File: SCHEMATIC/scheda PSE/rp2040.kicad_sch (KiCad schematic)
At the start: 26 parts, among them J1 Debug, SW1 RESET_SW, SW2 PROG_SW, U1 RP2040, U2 W25Q16JVUSSQ, U3 AT24C256, Y1 12MHz

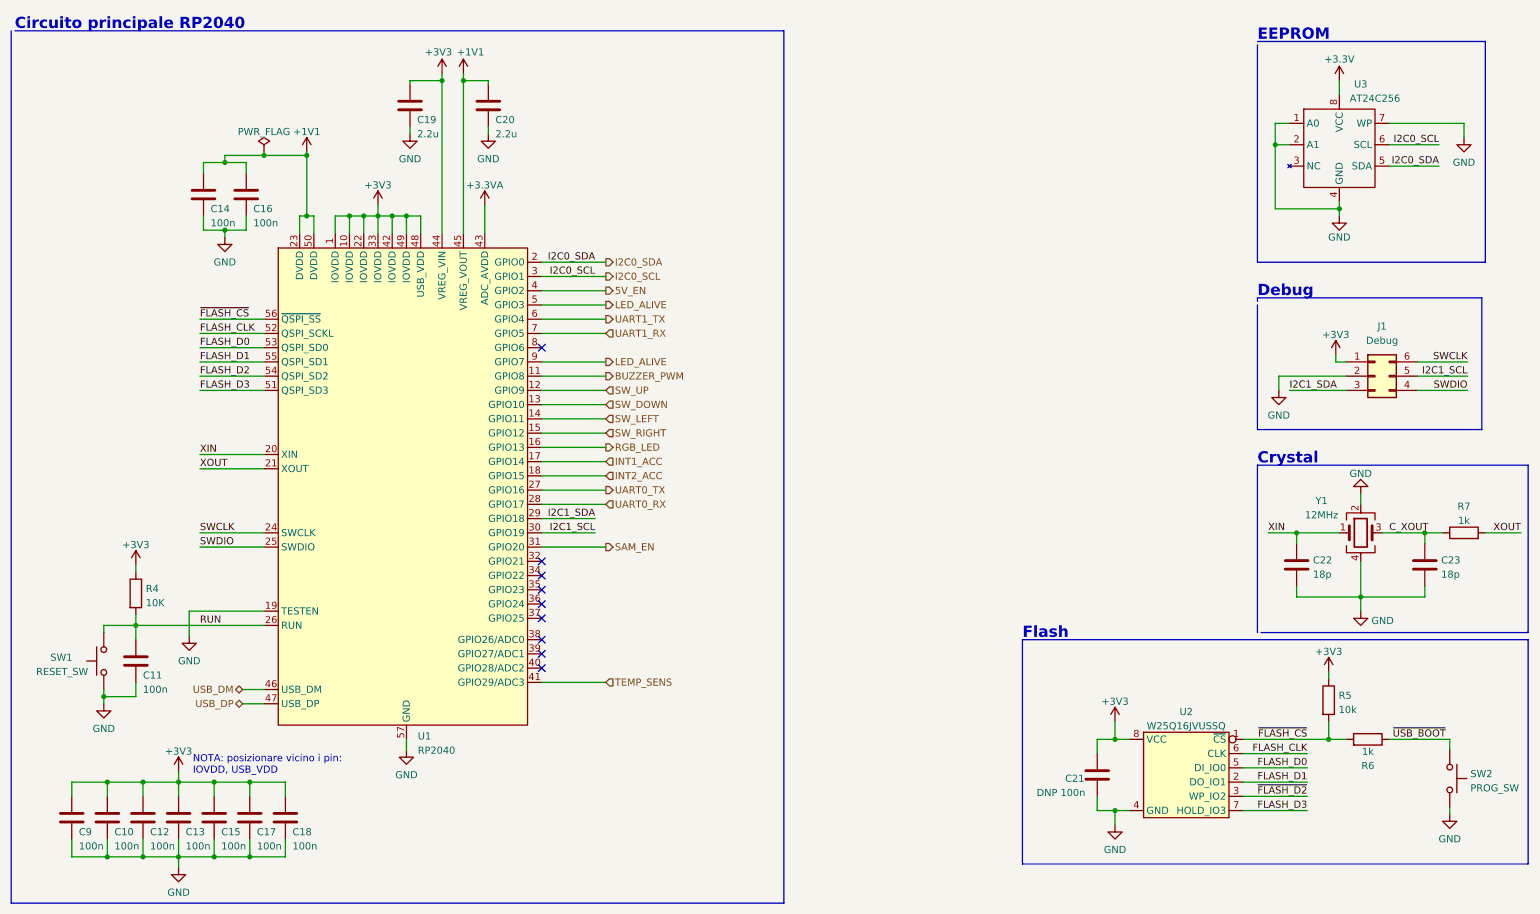
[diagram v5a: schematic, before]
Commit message: iniziato lo broglio. Prima di continuare modificare pin schema
iniziato lo sbroglio della scheda, prima di continuare bisogna sistemare i pin che siano concordi con quelli degli altro (ovvero sistemarli come da tabella su telegram)
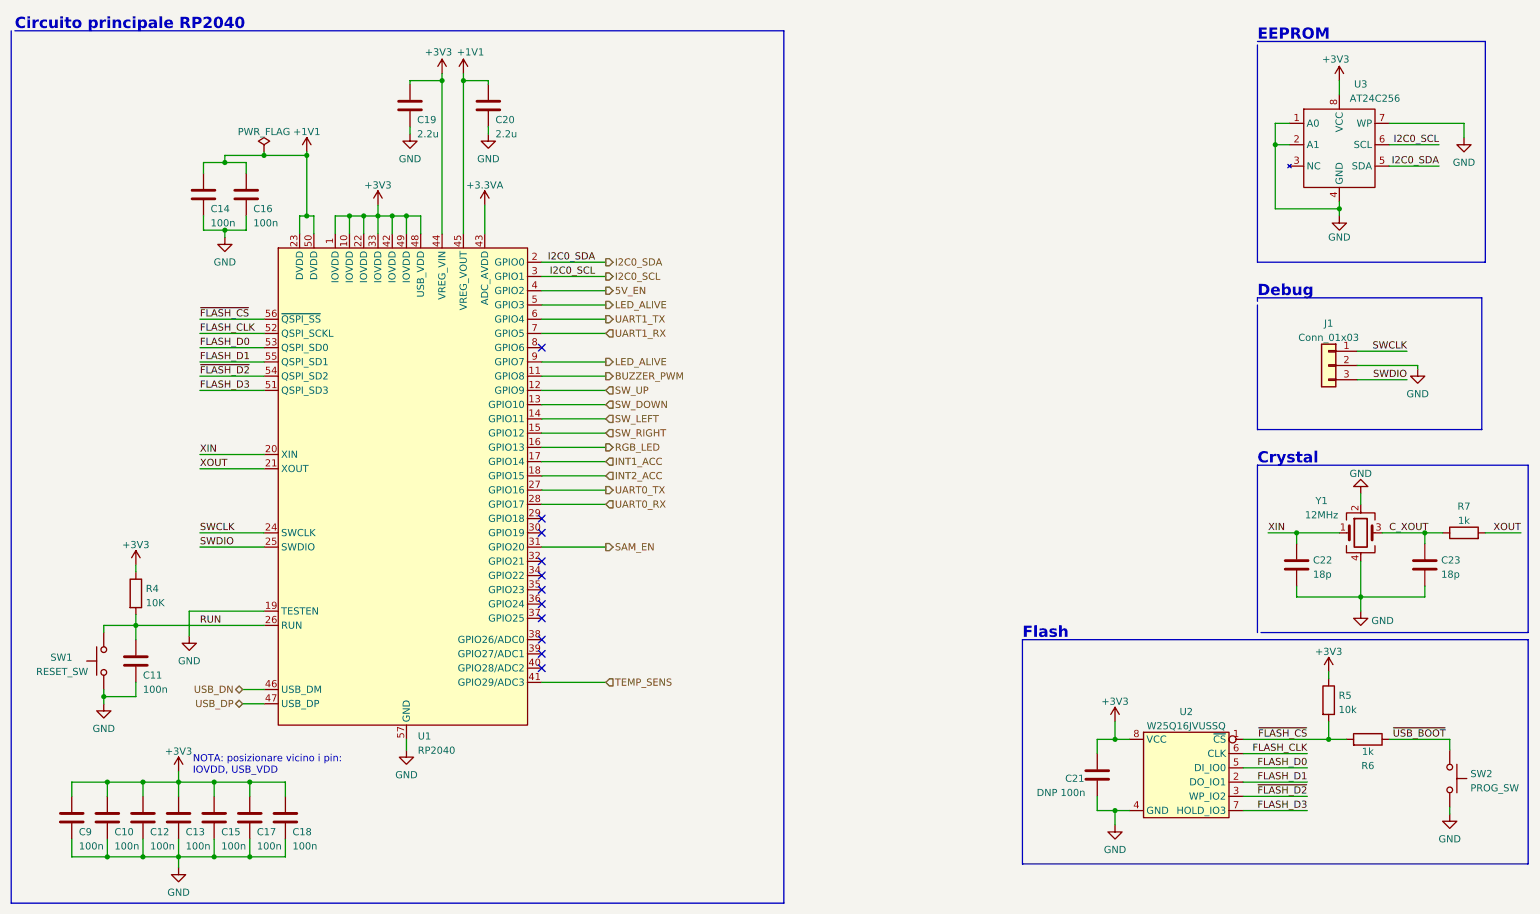
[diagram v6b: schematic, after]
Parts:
- removed J1: Debug, Connector_PinHeader_2.54mm:PinHeader_2x03_P2.54mm_Vertical, symbol Connector_Generic:Conn_02x03_Counter_Clockwise
- added J1: Conn_01x03, Connector_PinHeader_2.54mm:PinHeader_1x03_P2.54mm_Vertical, symbol Connector_Generic:Conn_01x03
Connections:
- net +3.3V is gone; now on net +3V3: U3.8 (VCC)
- net FLASH_D2 is gone; now on net ~{FLASH_D2}: U1.54 (QSPI_SD2)
- net GND: now also J1.2 (Pin_2)
- net SWCLK: now also J1.1 (Pin_1)
- net SWDIO: now also J1.3 (Pin_3)
- net I2C1_SCL: no longer names the net of U1.30 (GPIO19)
- net I2C1_SDA: no longer names the net of U1.29 (GPIO18)
- net USB_DM renamed USB_DN
- no-connect marks 9 -> 11

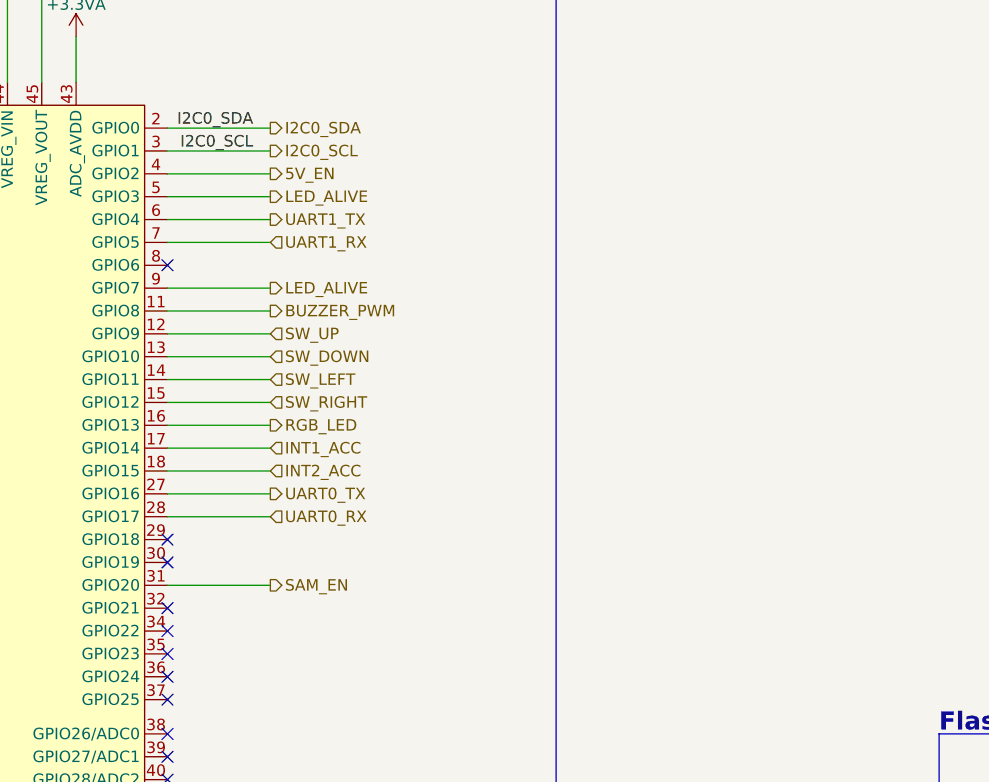
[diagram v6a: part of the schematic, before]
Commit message: modificato pin 2,3,14,15,16,17,18,27,28,29,30,31,32
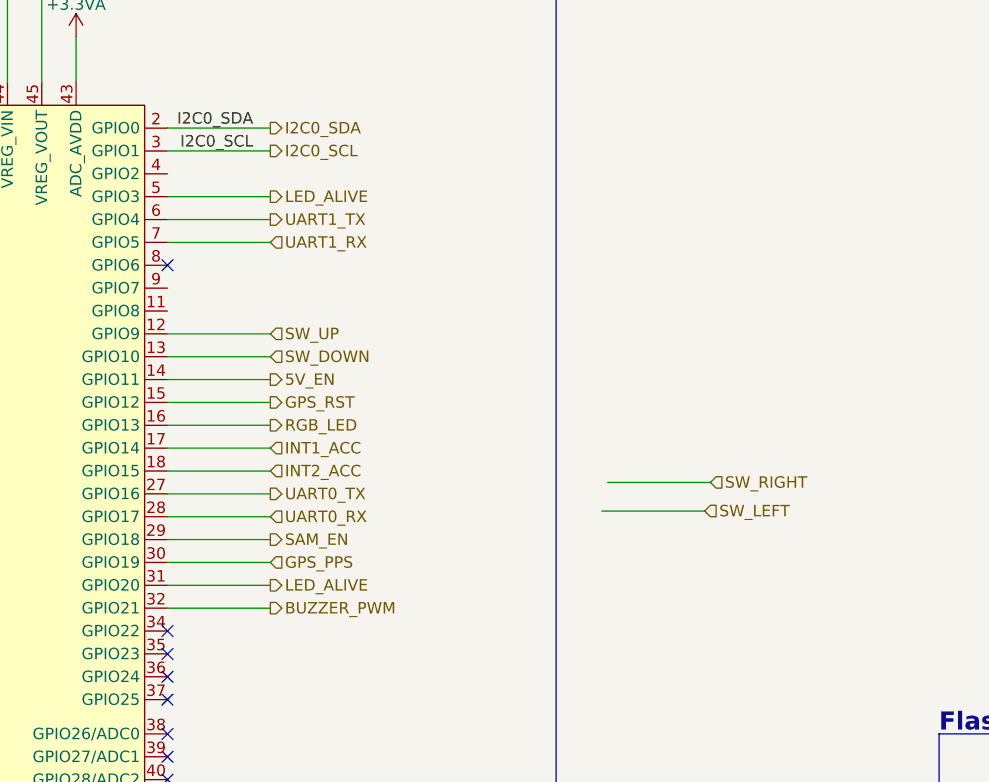
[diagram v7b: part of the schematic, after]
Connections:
- net 5V_EN: now also U1.14 (GPIO11); no longer U1.4 (GPIO2)
- net BUZZER_PWM: now also U1.32 (GPIO21); no longer U1.11 (GPIO8)
- net LED_ALIVE: now also U1.31 (GPIO20); no longer U1.9 (GPIO7)
- net SAM_EN: now also U1.29 (GPIO18); no longer U1.31 (GPIO20)
- net SW_LEFT: no longer U1.14 (GPIO11)
- net SW_RIGHT: no longer U1.15 (GPIO12)
- net GPS_PPS: now reaches U1.30 (GPIO19)
- new net GPS_RST: U1.15 (GPIO12)
- no-connect marks 11 -> 8

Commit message: finito lo sbroglio (magari da ricontrollare)
finito lo sbroglio, controllato già io ma meglio ridare una controllata.
Da sistemare tutta la serigrafia
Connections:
- net LED_ALIVE: no longer U1.5 (GPIO3)
- net SW_DOWN: now also U1.35 (GPIO23); no longer U1.13 (GPIO10)
- net SW_LEFT: now also U1.37 (GPIO25)
- net SW_RIGHT: now also U1.36 (GPIO24)
- net SW_UP: now also U1.34 (GPIO22); no longer U1.12 (GPIO9)
- net TEMP_SENS: now also U1.38 (GPIO26/ADC0); no longer U1.41 (GPIO29/ADC3)
- net SAM_EN renamed GPS_EN
- new net ACC_SA0: U1.13 (GPIO10)
- no-connect marks 8 -> 9
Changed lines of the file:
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@@
   (junction (at 55.88 163.83) (diameter 0) (color 0 0 0 0)
   )
-  (no_connect (at 107.95 116.205))
-  (no_connect (at 107.95 113.665))
+  (no_connect (at 107.95 127.635))
+  (no_connect (at 107.95 130.175))
+  (no_connect (at 107.95 132.715))
+  (no_connect (at 107.95 62.865))
   (no_connect (at 107.95 73.025))
-  (no_connect (at 107.95 130.175))
-  (no_connect (at 107.95 125.095))
-  (no_connect (at 107.95 121.285))
-  (no_connect (at 107.95 118.745))
-  (no_connect (at 107.95 127.635))
+  (no_connect (at 107.95 75.565))
+  (no_connect (at 107.95 78.105))
+  (no_connect (at 107.95 80.645))
+  (no_connect (at 107.95 65.405))
   (polyline (pts (xy 193.675 165.1) (xy 283.845 165.1))
     (stroke (width 0) (type default) (color 0 0 0 0))
@@
     (stroke (width 0) (type default) (color 0 0 0 0))
   )
-  (wire (pts (xy 107.95 132.715) (xy 119.38 132.715))
+  (wire (pts (xy 107.95 125.095) (xy 119.38 125.095))
     (stroke (width 0) (type default) (color 0 0 0 0))
   )
@@
     (stroke (width 0) (type default) (color 0 0 0 0))
   )
-  (wire (pts (xy 156.845 97.155) (xy 168.275 97.155))
+  (wire (pts (xy 107.95 118.745) (xy 119.38 118.745))
     (stroke (width 0) (type default) (color 0 0 0 0))
   )
@@
     (stroke (width 0) (type default) (color 0 0 0 0))
   )
+  (wire (pts (xy 107.95 83.185) (xy 119.38 83.185))
+    (stroke (width 0) (type default) (color 0 0 0 0))
+  )
   (wire (pts (xy 107.95 106.045) (xy 119.38 106.045))
     (stroke (width 0) (type default) (color 0 0 0 0))
@@
     (stroke (width 0) (type default) (color 0 0 0 0))
   )
-  (wire (pts (xy 107.95 80.645) (xy 119.38 80.645))
+  (wire (pts (xy 107.95 113.665) (xy 119.38 113.665))
     (stroke (width 0) (type default) (color 0 0 0 0))
   )
@@
     (stroke (width 0) (type default) (color 0 0 0 0))
   )
-  (wire (pts (xy 107.95 83.185) (xy 119.38 83.185))
+  (wire (pts (xy 107.95 116.205) (xy 119.38 116.205))
     (stroke (width 0) (type default) (color 0 0 0 0))
   )
@@
     (stroke (width 0) (type default) (color 0 0 0 0))
   )
-  (wire (pts (xy 107.95 65.405) (xy 119.38 65.405))
-    (stroke (width 0) (type default) (color 0 0 0 0))
-  )
   (wire (pts (xy 36.83 163.83) (xy 43.18 163.83))
     (stroke (width 0) (type default) (color 0 0 0 0))
@@
     (stroke (width 0) (type default) (color 0 0 0 0))
   )
-  (wire (pts (xy 156.21 100.33) (xy 167.64 100.33))
+  (wire (pts (xy 107.95 121.285) (xy 119.38 121.285))
     (stroke (width 0) (type default) (color 0 0 0 0))
   )
@@
     (effects (font (size 1.27 1.27)) (justify left))
   )
-  (hierarchical_label "TEMP_SENS" (shape input) (at 119.38 132.715 0)
+  (hierarchical_label "TEMP_SENS" (shape input) (at 119.38 125.095 0)
     (effects (font (size 1.27 1.27)) (justify left))
   )
@@
     (effects (font (size 1.27 1.27)) (justify left))
   )
-  (hierarchical_label "SW_DOWN" (shape input) (at 119.38 83.185 0)
+  (hierarchical_label "SW_DOWN" (shape input) (at 119.38 116.205 0)
     (effects (font (size 1.27 1.27)) (justify left))
   )
@@
     (effects (font (size 1.27 1.27)) (justify left))
   )
+  (hierarchical_label "ACC_SA0" (shape output) (at 119.38 83.185 0)
+    (effects (font (size 1.27 1.27)) (justify left))
+  )
   (hierarchical_label "RGB_LED" (shape output) (at 119.38 90.805 0)
     (effects (font (size 1.27 1.27)) (justify left))
   )
-  (hierarchical_label "SW_RIGHT" (shape input) (at 168.275 97.155 0)
-    (effects (font (size 1.27 1.27)) (justify left))
-  )
-  (hierarchical_label "SAM_EN" (shape output) (at 119.38 103.505 0)
+  (hierarchical_label "SW_RIGHT" (shape input) (at 119.38 118.745 0)
+    (effects (font (size 1.27 1.27)) (justify left))
+  )
+  (hierarchical_label "GPS_EN" (shape output) (at 119.38 103.505 0)
     (effects (font (size 1.27 1.27)) (justify left))
   )
@@
     (effects (font (size 1.27 1.27)) (justify left))
   )
-  (hierarchical_label "SW_LEFT" (shape input) (at 167.64 100.33 0)
-    (effects (font (size 1.27 1.27)) (justify left))
-  )
-  (hierarchical_label "SW_UP" (shape input) (at 119.38 80.645 0)
+  (hierarchical_label "SW_LEFT" (shape input) (at 119.38 121.285 0)
+    (effects (font (size 1.27 1.27)) (justify left))
+  )
+  (hierarchical_label "SW_UP" (shape input) (at 119.38 113.665 0)
     (effects (font (size 1.27 1.27)) (justify left))
   )
@@
     (effects (font (size 1.27 1.27)) (justify left))
   )
-  (hierarchical_label "LED_ALIVE" (shape output) (at 119.38 65.405 0)
-    (effects (font (size 1.27 1.27)) (justify left))
-  )
